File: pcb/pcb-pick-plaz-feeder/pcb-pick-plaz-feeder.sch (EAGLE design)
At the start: 59 parts, among them T1 MMBT2222, U1 LDO-1117, U2 STM32F030CCT6, U3 DRV8833PWPR, X1 PIN_1X1SMD_BIG_L, X2 PIN_1X1SMD_BIG_L, X3 PIN_1X1SMD_BIG_L, X4 PIN_1X1SMD_BIG_L, X5 PIN_5X1HD, X6 PIN_1X1SMD_BIG_L, X7 PIN_1X1SMD_BIG_L

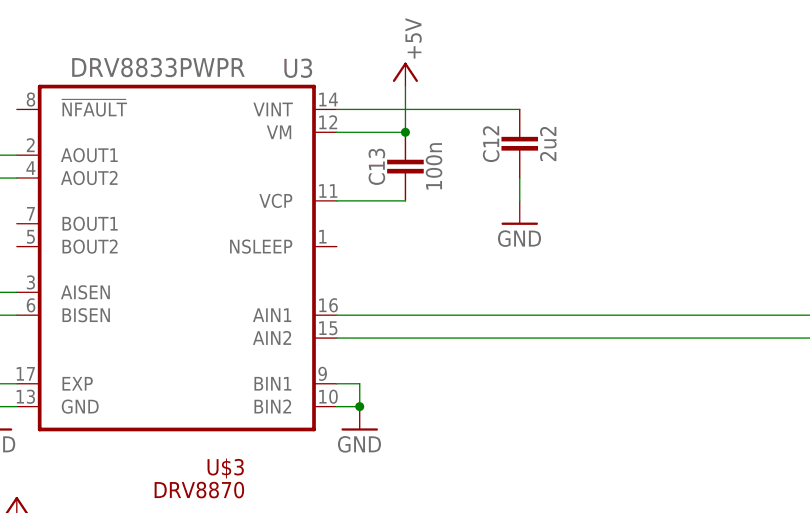
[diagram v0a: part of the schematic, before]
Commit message: updated pcbs with step files
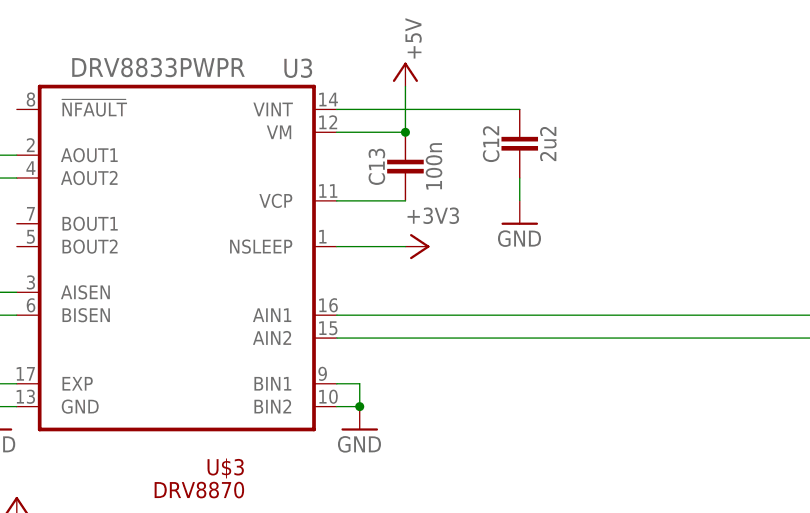
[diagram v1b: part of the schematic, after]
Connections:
- net +3V3: now also U3.NSLEEP
